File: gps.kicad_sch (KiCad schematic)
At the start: 16 parts, among them J2 Conn_Coaxial, U2 GY-NEO6MV2, U3 24AA32AT-I_SN

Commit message: ESC Update with Specifications
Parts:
- C10, C11, C9: value 0.1uF -> 100n
- C8: value 10uF -> 10u
- L3: value 27uH -> 27u
- renumbered J2 to Antenna
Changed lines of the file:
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@@
 	(wire
 		(pts
-			(xy 121.92 105.41) (xy 125.73 105.41)
+			(xy 121.92 105.41) (xy 132.08 105.41)
 		)
 		(stroke
@@
 	(wire
 		(pts
-			(xy 78.74 87.63) (xy 78.74 92.71)
+			(xy 78.74 81.28) (xy 78.74 92.71)
 		)
 		(stroke
@@
 	(wire
 		(pts
-			(xy 121.92 102.87) (xy 125.73 102.87)
+			(xy 121.92 102.87) (xy 132.08 102.87)
 		)
 		(stroke
@@
 		)
 	)
+	(label "GSDA"
+		(at 179.07 120.65 0)
+		(effects
+			(font
+				(size 1.27 1.27)
+			)
+			(justify left bottom)
+		)
+	)
 	(label "RF_In"
 		(at 149.86 125.73 180)
@@
 	)
 	(label "GSCl"
-		(at 184.15 113.03 270)
+		(at 186.69 113.03 0)
 		(effects
 			(font
 				(size 1.27 1.27)
 			)
-			(justify right bottom)
-		)
-	)
-	(label "GSDA"
-		(at 176.53 120.65 270)
-		(effects
-			(font
-				(size 1.27 1.27)
-			)
-			(justify right bottom)
+			(justify left bottom)
 		)
 	)
@@
 			)
 		)
-		(property "Value" "27uH"
+		(property "Value" "27u"
 			(at 157.734 123.698 0)
 			(effects
@@
 		(dnp no)
 		(fields_autoplaced yes)
-		(property "Reference" "J2"
+		(property "Reference" "Antenna"
 			(at 67.31 91.1467 0)
 			(effects
@@
 			(project "Drone V3"
 				(path "/6af311bf-2fb1-446c-8c7e-7c930a463809/72d226a8-57b5-4a0d-a5b2-83ff93ab3be7"
-					(reference "J2")
+					(reference "Antenna")
 					(unit 1)
 				)
@@
 		(on_board yes)
 		(dnp no)
-		(fields_autoplaced yes)
 		(property "Reference" "#PWR023"
 			(at 180.34 102.87 0)
@@
 		)
 		(property "Value" "+3V3"
-			(at 180.34 93.98 0)
+			(at 180.34 95.25 0)
 			(effects
 				(font
@@
 			)
 		)
-		(property "Value" "0.1uF"
+		(property "Value" "100n"
 			(at 243.84 114.2999 0)
 			(effects
@@
 			)
 		)
-		(property "Value" "0.1uF"
+		(property "Value" "100n"
 			(at 207.01 74.93 0)
 			(effects
@@
 		(dnp no)
 		(property "Reference" "R2"
-			(at 125.222 89.408 90)
+			(at 125.222 89.154 90)
 			(effects
 				(font
@@
 		)
 		(property "Value" "1k"
-			(at 128.524 89.408 90)
+			(at 128.524 89.154 90)
 			(effects
 				(font
@@
 			)
 		)
-		(property "Value" "10uF"
+		(property "Value" "10u"
 			(at 186.436 74.93 0)
 			(effects
@@
 			)
 		)
-		(property "Value" "0.1uF"
+		(property "Value" "100n"
 			(at 196.85 74.93 0)
 			(effects

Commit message: ESC Update & Finalization Draft
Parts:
- Antenna: footprint (none) -> Connector_Coaxial:U.FL_Hirose_U.FL-R-SMT-1_Vertical
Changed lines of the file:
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@@
 			)
 		)
-		(property "Footprint" ""
+		(property "Footprint" "Connector_Coaxial:U.FL_Hirose_U.FL-R-SMT-1_Vertical"
 			(at 71.12 92.71 0)
 			(effects

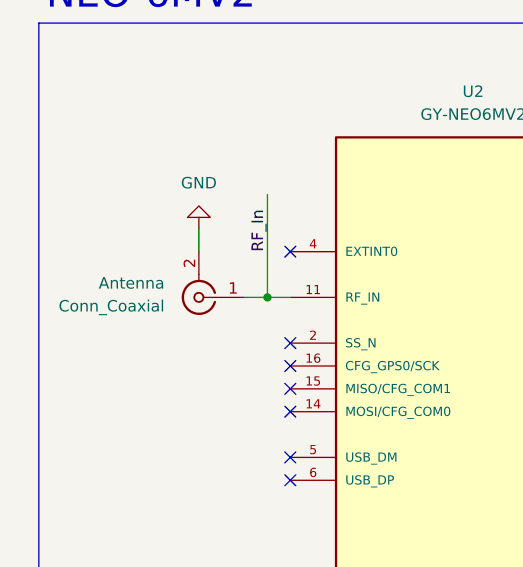
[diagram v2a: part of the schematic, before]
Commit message: Less bulky switching regulator for the ESC drivers, PCB update.
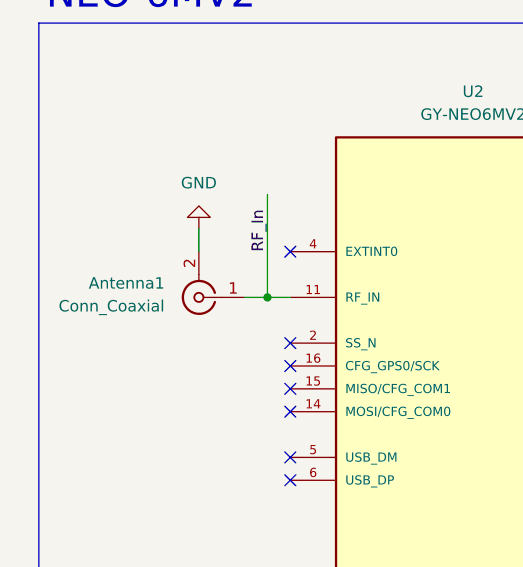
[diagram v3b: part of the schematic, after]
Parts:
- renumbered Antenna to Antenna1
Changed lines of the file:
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@@
 		(dnp no)
 		(fields_autoplaced yes)
-		(property "Reference" "Antenna"
+		(property "Reference" "Antenna1"
 			(at 67.31 91.1467 0)
 			(effects
@@
 			(project "Drone V3"
 				(path "/6af311bf-2fb1-446c-8c7e-7c930a463809/72d226a8-57b5-4a0d-a5b2-83ff93ab3be7"
-					(reference "Antenna")
+					(reference "Antenna1")
 					(unit 1)
 				)

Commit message: Sensors & Main board start
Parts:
- removed Antenna1: Conn_Coaxial, Connector_Coaxial:U.FL_Hirose_U.FL-R-SMT-1_Vertical, symbol Connector:Conn_Coaxial
- removed BT1: MS621FE, MS621FE-FL11E:BAT_MS621FE-FL11E, symbol MS621FE-FL11E:MS621FE-FL11E
- removed C10, C11, C9: 100n, symbol Device:C
- removed C8: 10u, symbol Device:C
- removed D2: BAT54S, Package_TO_SOT_SMD:SOT-23, symbol Diode:BAT54S
- removed D3: LED, symbol Device:LED
- removed L3: 27u, symbol Device:L
- removed R2: 1k, symbol Device:R
- removed R3: 22, symbol Device:R
- removed R4: 4.7k, symbol Device:R
- removed U2: GY-NEO6MV2, GY-NEO6MV2:XCVR_GY-NEO6MV2, symbol GY-NEO6MV2:GY-NEO6MV2
- removed U3: 24AA32AT-I_SN, 24AA32AT-I_SN:SOIC127P600X175-8N, symbol 24AA32AT-I_SN:24AA32AT-I_SN
- added D2: GPS_LED, symbol Device:LED
- added R39: 4.7k, symbol Device:R
- added U: PA1010D1, symbol CustomFPs:Adafruit_Mini_GPS_PA1010D
- R1: value 1k -> 220
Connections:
- net GND: now also D2.1 (K), U.1 (GND)
- net GPS_RX: now also U.6 (RXI)
- net GPS_TX: now also U.7 (TXO)
- net at R1.1: now also U.3 (3V3o)
- net at R1.2: now also D2.2 (A)
- net +3V3 renamed +3.3V
- net +3.3V: now also R39.1, U.2 (VIN)
- net GSDA renamed GPS_SCL
- net GPS_SCL: now also U.4 (SCL)
- new net GPS_SDA: R39.2, U.5 (SDA)
- no-connect marks 10 -> 0
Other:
- note added: "Requires 30mA Power Supply"
- note removed: "Decoupling"
- note removed: "EEPROM"
- note removed: "NEO-6MV2"

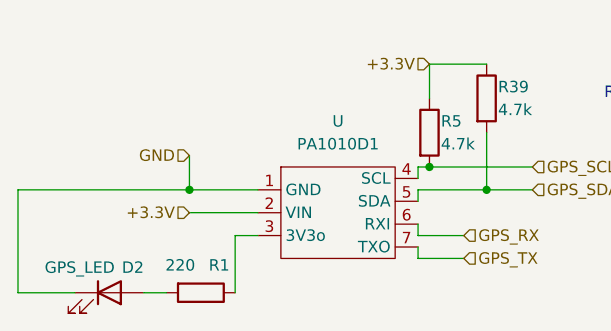
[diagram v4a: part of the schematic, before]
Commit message: MCU implementation start Still needs component schematic checks & component integration with MCU
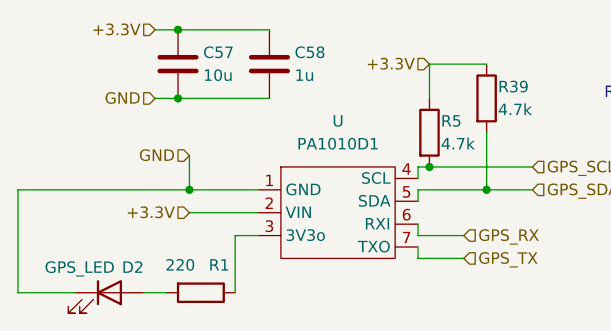
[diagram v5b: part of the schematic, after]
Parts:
- added C57: 10u, symbol Device:C
- added C58: 1u, symbol Device:C
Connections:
- net +3.3V: now also C57.1, C58.1
- net GND: now also C57.2, C58.2
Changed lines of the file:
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@@
 		(color 0 0 0 0)
 	)
+	(junction
+		(at 129.54 85.09)
+		(diameter 0)
+		(color 0 0 0 0)
+	)
+	(junction
+		(at 129.54 77.47)
+		(diameter 0)
+		(color 0 0 0 0)
+	)
 	(wire
 		(pts
@@
 	(wire
 		(pts
+			(xy 129.54 85.09) (xy 139.7 85.09)
+		)
+		(stroke
+			(width 0)
+			(type default)
+		)
+	)
+	(wire
+		(pts
 			(xy 125.73 106.68) (xy 128.27 106.68)
 		)
@@
 	(wire
 		(pts
+			(xy 127 85.09) (xy 129.54 85.09)
+		)
+		(stroke
+			(width 0)
+			(type default)
+		)
+	)
+	(wire
+		(pts
 			(xy 161.29 102.87) (xy 156.21 102.87)
 		)
@@
 		(pts
 			(xy 135.89 100.33) (xy 138.43 100.33)
+		)
+		(stroke
+			(width 0)
+			(type default)
+		)
+	)
+	(wire
+		(pts
+			(xy 127 77.47) (xy 129.54 77.47)
+		)
+		(stroke
+			(width 0)
+			(type default)
+		)
+	)
+	(wire
+		(pts
+			(xy 129.54 77.47) (xy 139.7 77.47)
 		)
 		(stroke
@@
 		)
 	)
+	(hierarchical_label "GND"
+		(shape input)
+		(at 127 85.09 180)
+		(effects
+			(font
+				(size 1.27 1.27)
+			)
+			(justify right)
+		)
+	)
 	(hierarchical_label "GPS_RX"
 		(shape input)
@@
 		(shape input)
 		(at 130.81 97.79 180)
+		(effects
+			(font
+				(size 1.27 1.27)
+			)
+			(justify right)
+		)
+	)
+	(hierarchical_label "+3.3V"
+		(shape input)
+		(at 127 77.47 180)
 		(effects
 			(font
@@
 				(path "/6af311bf-2fb1-446c-8c7e-7c930a463809/72d226a8-57b5-4a0d-a5b2-83ff93ab3be7"
 					(reference "R5")
+					(unit 1)
+				)
+			)
+		)
+	)
+	(symbol
+		(lib_id "Device:C")
+		(at 139.7 81.28 0)
+		(unit 1)
+		(exclude_from_sim no)
+		(in_bom yes)
+		(on_board yes)
+		(dnp no)
+		(property "Reference" "C58"
+			(at 142.494 80.01 0)
+			(effects
+				(font
+					(size 1.27 1.27)
+				)
+				(justify left)
+			)
+		)
+		(property "Value" "1u"
+			(at 142.494 82.55 0)
+			(effects
+				(font
+					(size 1.27 1.27)
+				)
+				(justify left)
+			)
+		)
+		(property "Footprint" ""
+			(at 140.6652 85.09 0)
+			(effects
+				(font
+					(size 1.27 1.27)
+				)
+				(hide yes)
+			)
+		)
+		(property "Datasheet" "~"
+			(at 139.7 81.28 0)
+			(effects
+				(font
+					(size 1.27 1.27)
+				)
+				(hide yes)
+			)
+		)
+		(property "Description" "Unpolarized capacitor"
+			(at 139.7 81.28 0)
+			(effects
+				(font
+					(size 1.27 1.27)
+				)
+				(hide yes)
+			)
+		)
+		(pin "1"
+		)
+		(pin "2"
+		)
+		(instances
+			(project "Drone V3"
+				(path "/6af311bf-2fb1-446c-8c7e-7c930a463809/72d226a8-57b5-4a0d-a5b2-83ff93ab3be7"
+					(reference "C58")
 					(unit 1)
 				)
@@
 					(unit 1)
 				)
+			)
+		)
+	)
+	(symbol
+		(lib_id "Device:C")
+		(at 129.54 81.28 0)
+		(unit 1)
+		(exclude_from_sim no)
+		(in_bom yes)
+		(on_board yes)
+		(dnp no)
+		(property "Reference" "C57"
+			(at 132.334 80.01 0)
+			(effects
+				(font
+					(size 1.27 1.27)
+				)
+				(justify left)
+			)
+		)
+		(property "Value" "10u"
+			(at 132.334 82.55 0)
+			(effects
+				(font
+					(size 1.27 1.27)
+				)
+				(justify left)
+			)
+		)
+		(property "Footprint" ""
+			(at 130.5052 85.09 0)
+			(effects
+				(font
+					(size 1.27 1.27)
+				)
+				(hide yes)
+			)
+		)
+		(property "Datasheet" "~"
+			(at 129.54 81.28 0)
+			(effects
+				(font
+					(size 1.27 1.27)
+				)
+				(hide yes)
+			)
+		)
+		(property "Description" "Unpolarized capacitor"
+			(at 129.54 81.28 0)
+			(effects
+				(font
+					(size 1.27 1.27)
+				)
+				(hide yes)
+			)
+		)
+		(pin "1"
+		)
+		(pin "2"
+		)
+		(instances
+			(project ""
+				(path "/6af311bf-2fb1-446c-8c7e-7c930a463809/72d226a8-57b5-4a0d-a5b2-83ff93ab3be7"
+					(reference "C57")
+					(unit 1)
+				)

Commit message: GPS Schematic Update
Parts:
- removed R39, R5: 4.7k, symbol Device:R
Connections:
- net GPS_SCL: no longer names the net of U.4 (SCL)
- net GPS_SDA: no longer names the net of U.5 (SDA)
- no-connect marks 0 -> 2
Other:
- note removed: "Requires 30mA Power Supply"
